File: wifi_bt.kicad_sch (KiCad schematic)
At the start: 41 parts, among them J3 U_FL-R-SMT-1, U25 NTS0102_XSON, U26 WiFi_Bluetooth_LBEE5PK2AE, U27 NTS0102_XSON, U29 NTS0102_XSON, U30 NTS0102_XSON, Y4 Oscillator_32.768kHz_ECS_2520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

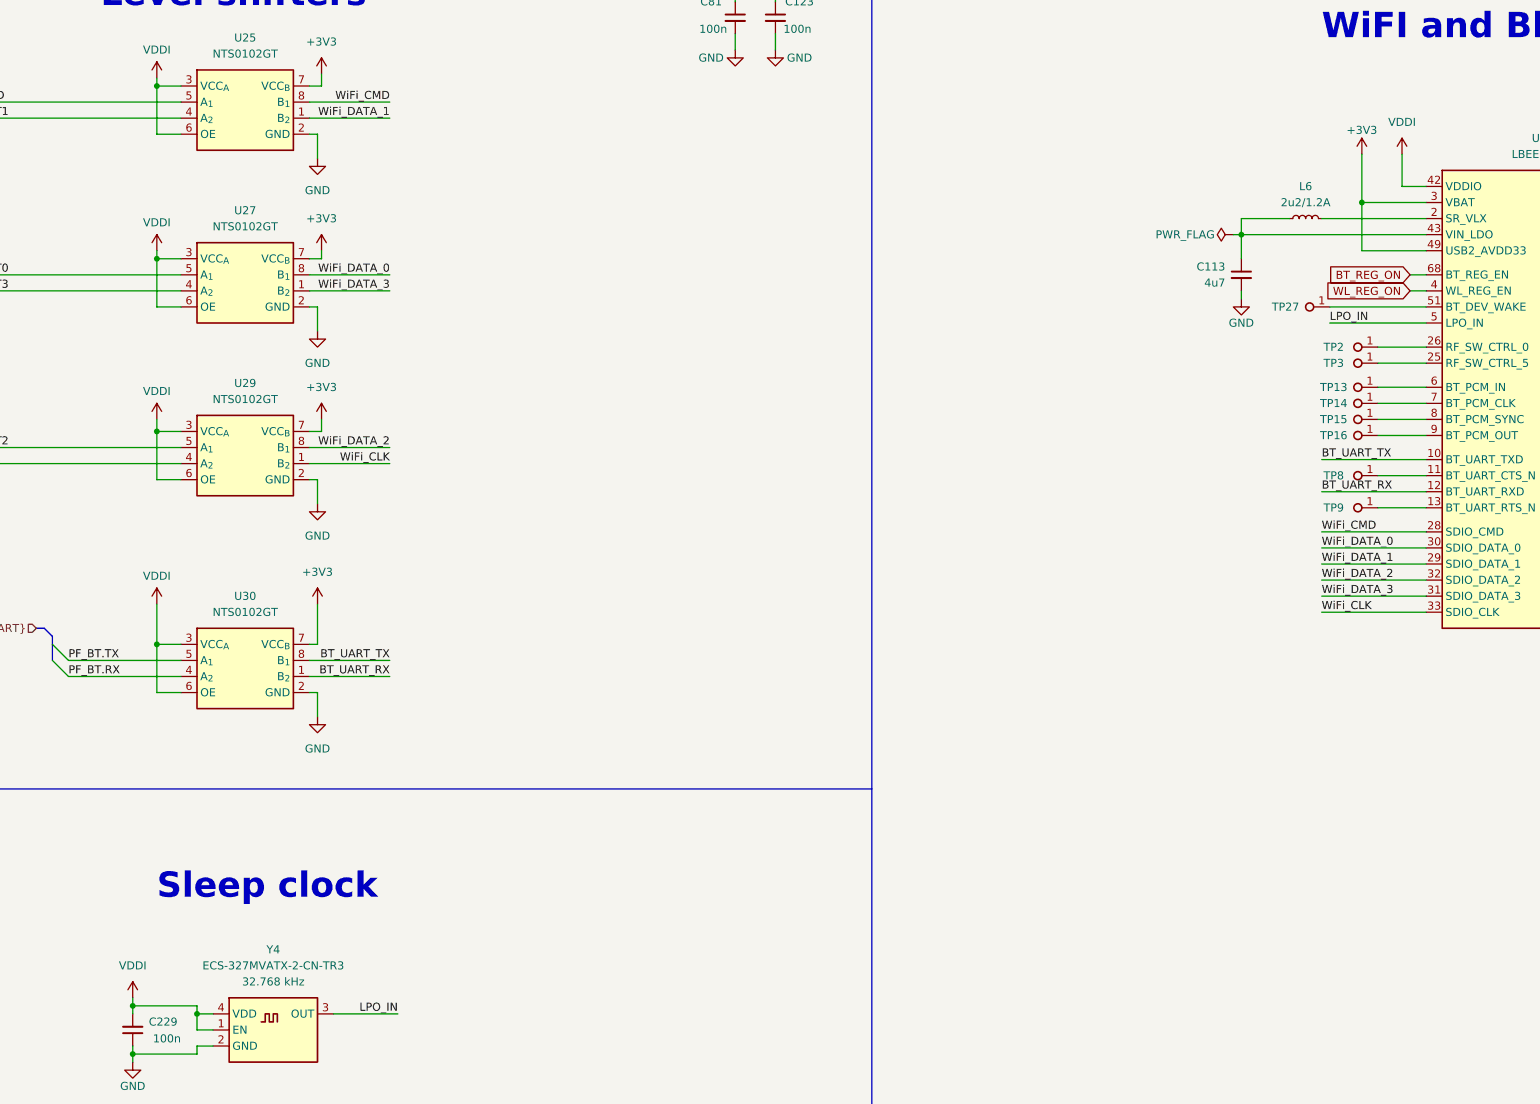
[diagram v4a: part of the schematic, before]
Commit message: [#57422] Change WL_BT modules VDDIO to 3V3
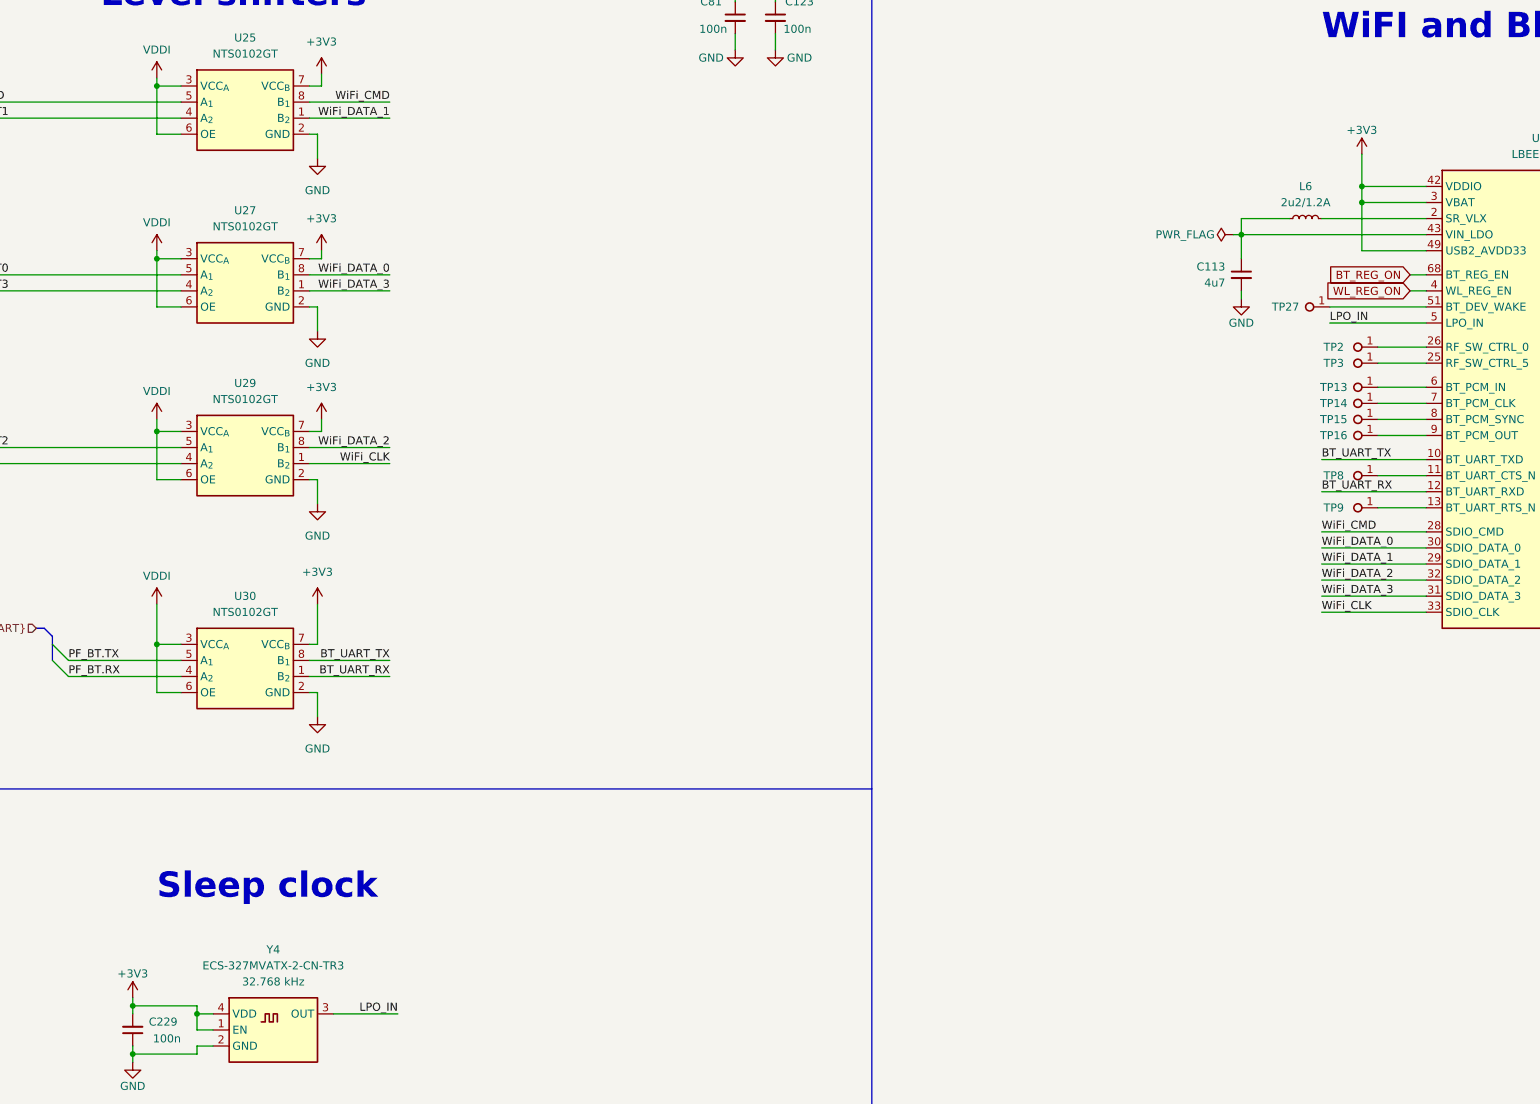
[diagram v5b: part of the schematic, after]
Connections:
- net +3V3: now also C229.2, U26.42 (VDDIO), Y4.1 (EN), Y4.4 (VDD)
- net VDDI: no longer C229.2, U26.42 (VDDIO), Y4.1 (EN), Y4.4 (VDD)
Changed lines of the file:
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@@
   (junction (at 107.315 40.005) (diameter 0) (color 0 0 0 0)
   )
+  (junction (at 279.4 116.84) (diameter 0) (color 0 0 0 0)
+  )
   (no_connect (at 327.66 167.64))
   (bus_entry (at 56.515 133.35) (size -2.54 -2.54)
@@
     (stroke (width 0) (type default))
   )
-  (wire (pts (xy 285.75 111.76) (xy 285.75 116.84))
-    (stroke (width 0) (type default))
-  )
   (wire (pts (xy 114.935 100.965) (xy 113.03 100.965))
     (stroke (width 0) (type default))
@@
     (stroke (width 0) (type default))
   )
-  (wire (pts (xy 279.4 111.76) (xy 279.4 119.38))
+  (wire (pts (xy 279.4 111.76) (xy 279.4 116.84))
     (stroke (width 0) (type default))
   )
@@
     (stroke (width 0) (type default))
   )
-  (wire (pts (xy 285.75 116.84) (xy 289.56 116.84))
+  (wire (pts (xy 279.4 116.84) (xy 289.56 116.84))
     (stroke (width 0) (type default))
   )
@@
     (stroke (width 0) (type default))
   )
+  (wire (pts (xy 279.4 116.84) (xy 279.4 119.38))
+    (stroke (width 0) (type default))
+  )
   (wire (pts (xy 41.275 38.735) (xy 41.275 40.005))
     (stroke (width 0) (type default))
@@
     )
   )
-  (symbol (lib_id "antmicropower:VDDI") (at 285.75 111.76 0) (unit 1)
-    (in_bom yes) (on_board yes) (dnp no) (fields_autoplaced)
-    (property "Reference" "#PWR0348" (at 285.75 115.57 0)
-      (effects (font (size 1.27 1.27)) hide)
-    )
-    (property "Value" "VDDI" (at 285.75 106.68 0)
-      (effects (font (size 1.27 1.27)))
-    )
-    (property "Footprint" "" (at 285.75 111.76 0)
-      (effects (font (size 1.27 1.27)) hide)
-    )
-    (property "Datasheet" "" (at 285.75 111.76 0)
-      (effects (font (size 1.27 1.27)) hide)
-    )
-    (pin "1")
-    (instances
-      (project "polarfire-som"
-        (path "/db4a0d3e-2eb3-499e-977d-6eb378cfd3ed/8b90881e-9aeb-4751-9bcc-bff3e303e2ab"
-          (reference "#PWR0348") (unit 1)
-        )
-      )
-    )
-  )
   (symbol (lib_id "antmicropower:+3V3") (at 114.935 99.06 0) (mirror y) (unit 1)
     (in_bom yes) (on_board yes) (dnp no) (fields_autoplaced)
@@
     )
   )
-  (symbol (lib_id "antmicropower:VDDI") (at 85.09 245.11 0) (unit 1)
-    (in_bom yes) (on_board yes) (dnp no) (fields_autoplaced)
-    (property "Reference" "#PWR0347" (at 85.09 248.92 0)
-      (effects (font (size 1.27 1.27)) hide)
-    )
-    (property "Value" "VDDI" (at 85.09 240.03 0)
-      (effects (font (size 1.27 1.27)))
-    )
-    (property "Footprint" "" (at 85.09 245.11 0)
-      (effects (font (size 1.27 1.27)) hide)
-    )
-    (property "Datasheet" "" (at 85.09 245.11 0)
-      (effects (font (size 1.27 1.27)) hide)
-    )
-    (pin "1")
-    (instances
-      (project "polarfire-som"
-        (path "/db4a0d3e-2eb3-499e-977d-6eb378cfd3ed/8b90881e-9aeb-4751-9bcc-bff3e303e2ab"
-          (reference "#PWR0347") (unit 1)
-        )
-      )
-    )
-  )
   (symbol (lib_id "antmicropower:+3V3") (at 114.3 182.88 0) (mirror y) (unit 1)
     (in_bom yes) (on_board yes) (dnp no) (fields_autoplaced)
@@
         )
       )
+    )
+  )
+  (symbol (lib_id "antmicropower:+3V3") (at 85.09 245.11 0) (unit 1)
+    (in_bom yes) (on_board yes) (dnp no)
+    (property "Reference" "#PWR0347" (at 100.33 247.65 0)
+      (effects (font (size 1.27 1.27) (thickness 0.15)) (justify left bottom) hide)
+    )
+    (property "Value" "+3V3" (at 85.09 241.3 0)
+      (effects (font (size 1.27 1.27) (thickness 0.15)))
+    )
+    (property "Footprint" "" (at 100.33 252.73 0)
+      (effects (font (size 1.27 1.27) (thickness 0.15)) (justify left bottom) hide)
+    )
+    (property "Datasheet" "" (at 100.33 255.27 0)
+      (effects (font (size 1.27 1.27) (thickness 0.15)) (justify left bottom) hide)
+    )
+    (property "Author" "Antmicro" (at 100.33 252.73 0)
+      (effects (font (size 1.27 1.27) (thickness 0.15)) (justify left bottom) hide)
+    )
+    (property "License" "Apache-2.0" (at 100.33 255.27 0)
+      (effects (font (size 1.27 1.27) (thickness 0.15)) (justify left bottom) hide)
+    )
+    (pin "1")
+    (instances
+      (project "polarfire-som"
+        (path "/db4a0d3e-2eb3-499e-977d-6eb378cfd3ed/8b90881e-9aeb-4751-9bcc-bff3e303e2ab"
+          (reference "#PWR0347") (unit 1)
+        )
+      )

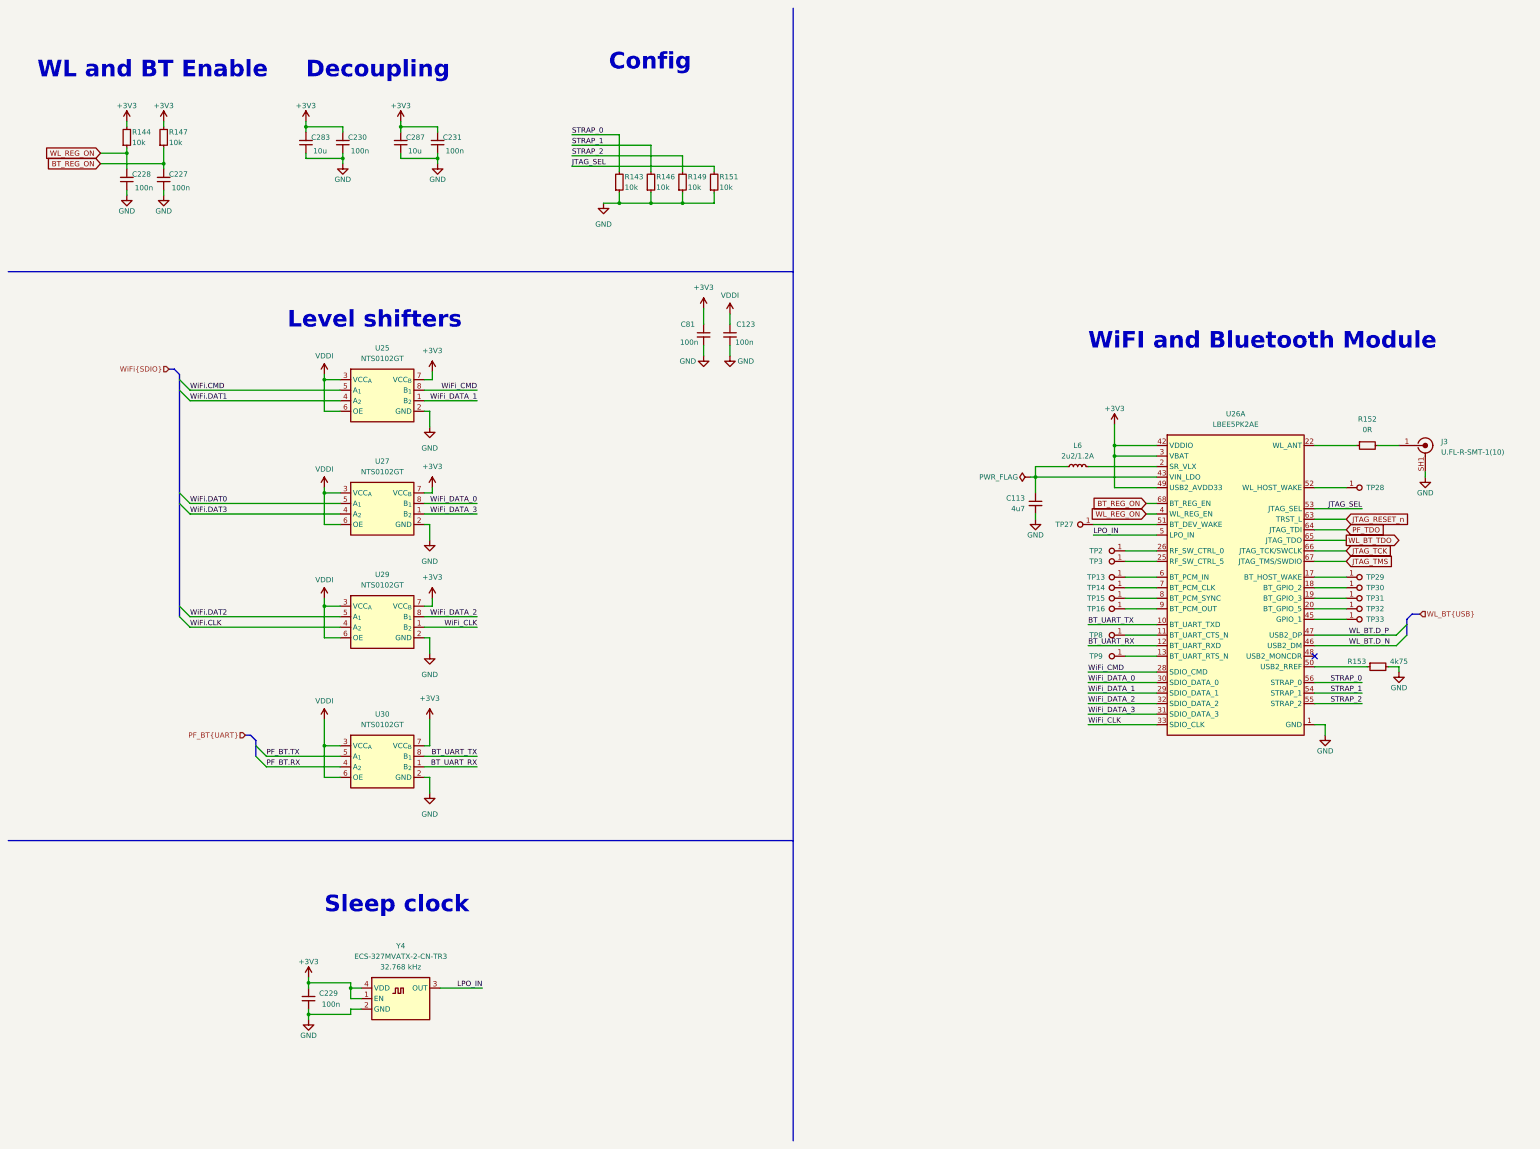
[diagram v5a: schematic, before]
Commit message: [#57505] Finish migration to hierarchical structure
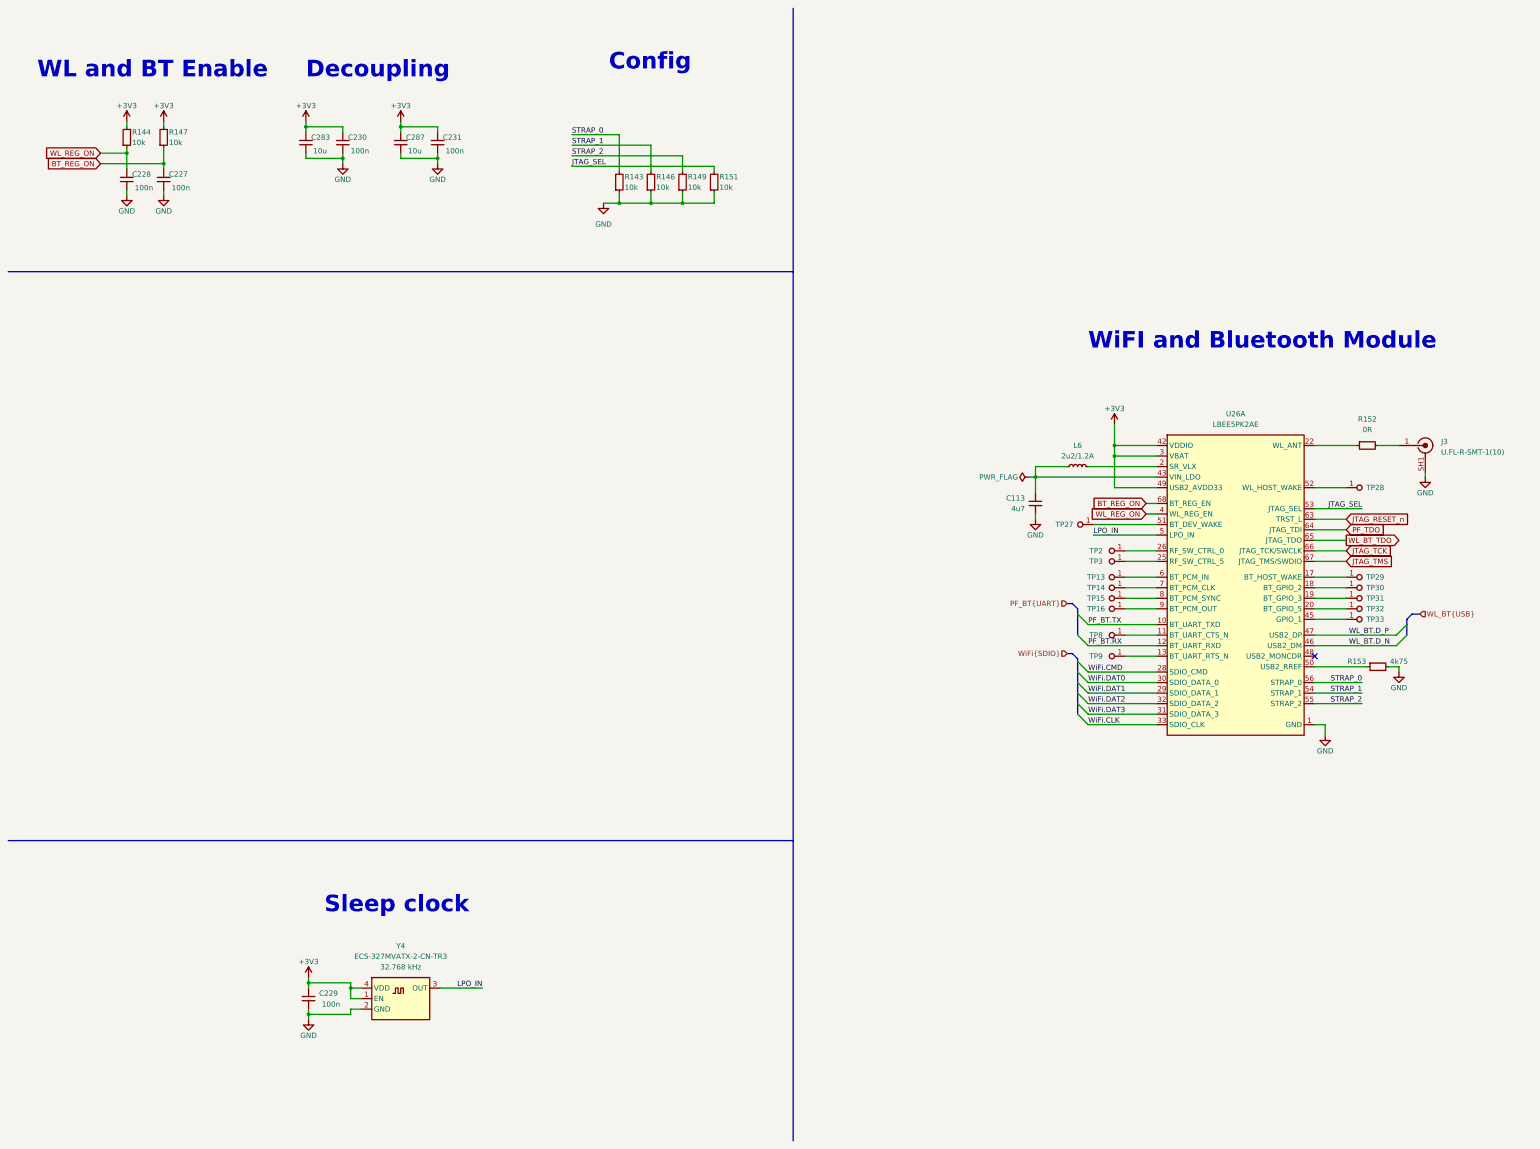
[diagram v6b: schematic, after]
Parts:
- removed C123, C81: C_100n_0402, antmicro-footprints:C_0402_1005Metric, symbol antmicroCapacitors0402:C_100n_0402
- removed U25, U27, U29, U30: NTS0102_XSON, antmicro-footprints:XSON-8_1x1.95mm_P0.5mm, symbol antmicroLogicTranslatorsLevelShifters:NTS0102_XSON
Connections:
- net BT_UART_RX is gone; now on net PF_BT.RX: U26.12 (BT_UART_RXD)
- net BT_UART_TX is gone; now on net PF_BT.TX: U26.10 (BT_UART_TXD)
- net WiFi_CLK is gone; now on net WiFi.CLK: U26.33 (SDIO_CLK)
- net WiFi_CMD is gone; now on net WiFi.CMD: U26.28 (SDIO_CMD)
- net WiFi_DATA_0 is gone; now on net WiFi.DAT0: U26.30 (SDIO_DATA_0)
- net WiFi_DATA_1 is gone; now on net WiFi.DAT1: U26.29 (SDIO_DATA_1)
- net WiFi_DATA_2 is gone; now on net WiFi.DAT2: U26.32 (SDIO_DATA_2)
- net WiFi_DATA_3 is gone; now on net WiFi.DAT3: U26.31 (SDIO_DATA_3)
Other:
- note removed: "Level shifters"

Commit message: [#57422] Finishing touches
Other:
- moved on the sheet: C113, C227, C228, C229, C230, C231, C283, C287, J3, L6, R143, R144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

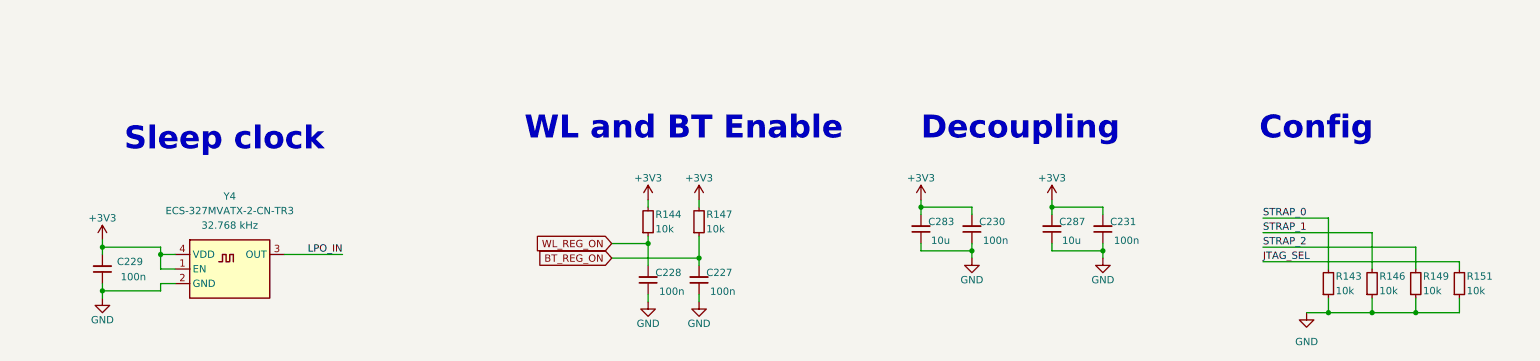
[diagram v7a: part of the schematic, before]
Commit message: [#57422] Align schematics
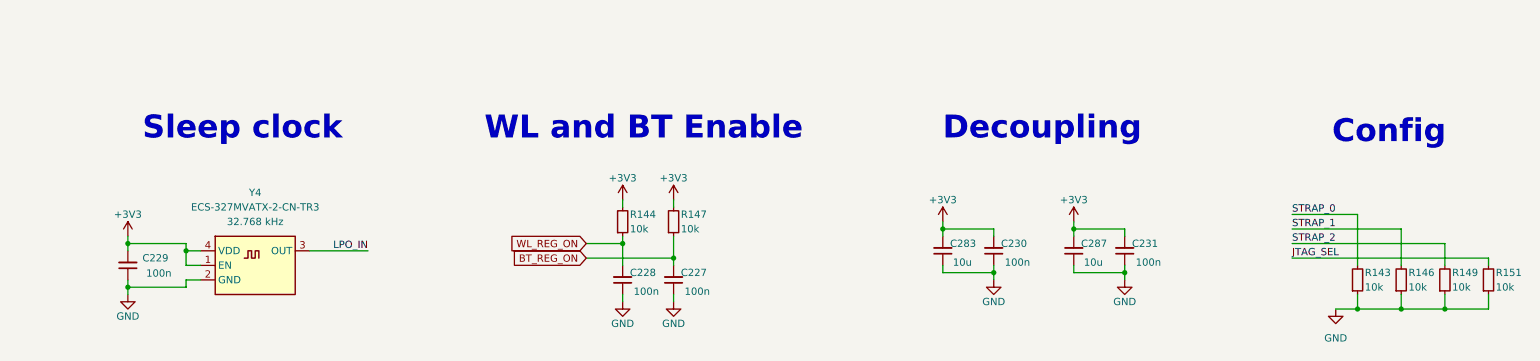
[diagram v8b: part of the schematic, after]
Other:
- moved on the sheet: C227, C228, C229, C230, C231, C283, C287, R143, R144, R146, R147, R149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
